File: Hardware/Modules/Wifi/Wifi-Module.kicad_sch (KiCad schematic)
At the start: 9 parts, among them J3 Conn_01x01_Pin, J4 B4B-EH-A, J5 Conn_01x10, J6 Conn_01x10, J7 B4B-EH-A, U1 ESP32-C6-MINI-1-H4, U2 TLV70033_SOT23-5

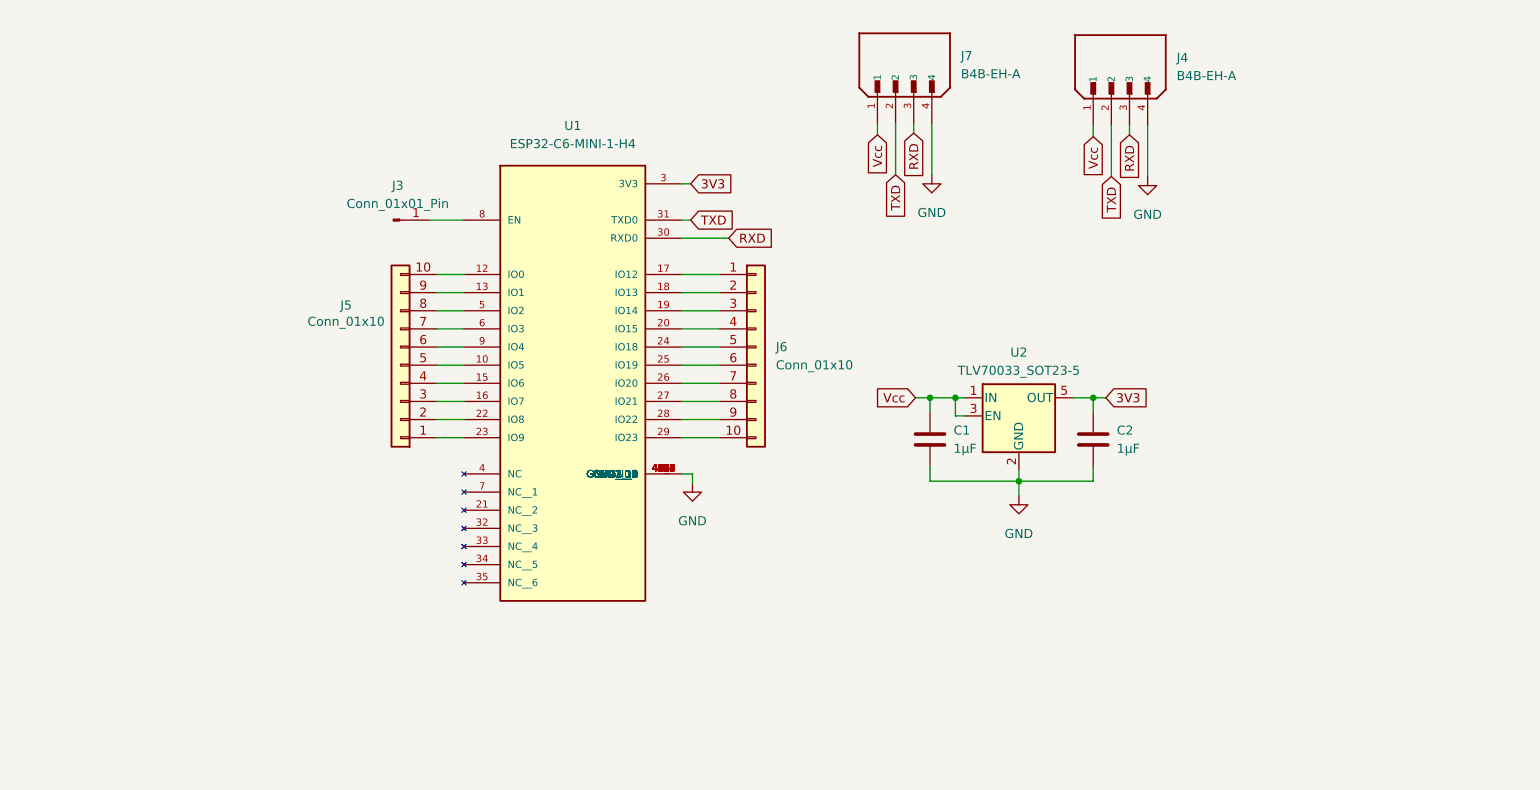
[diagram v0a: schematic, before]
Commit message: Correction in the Wifi Module
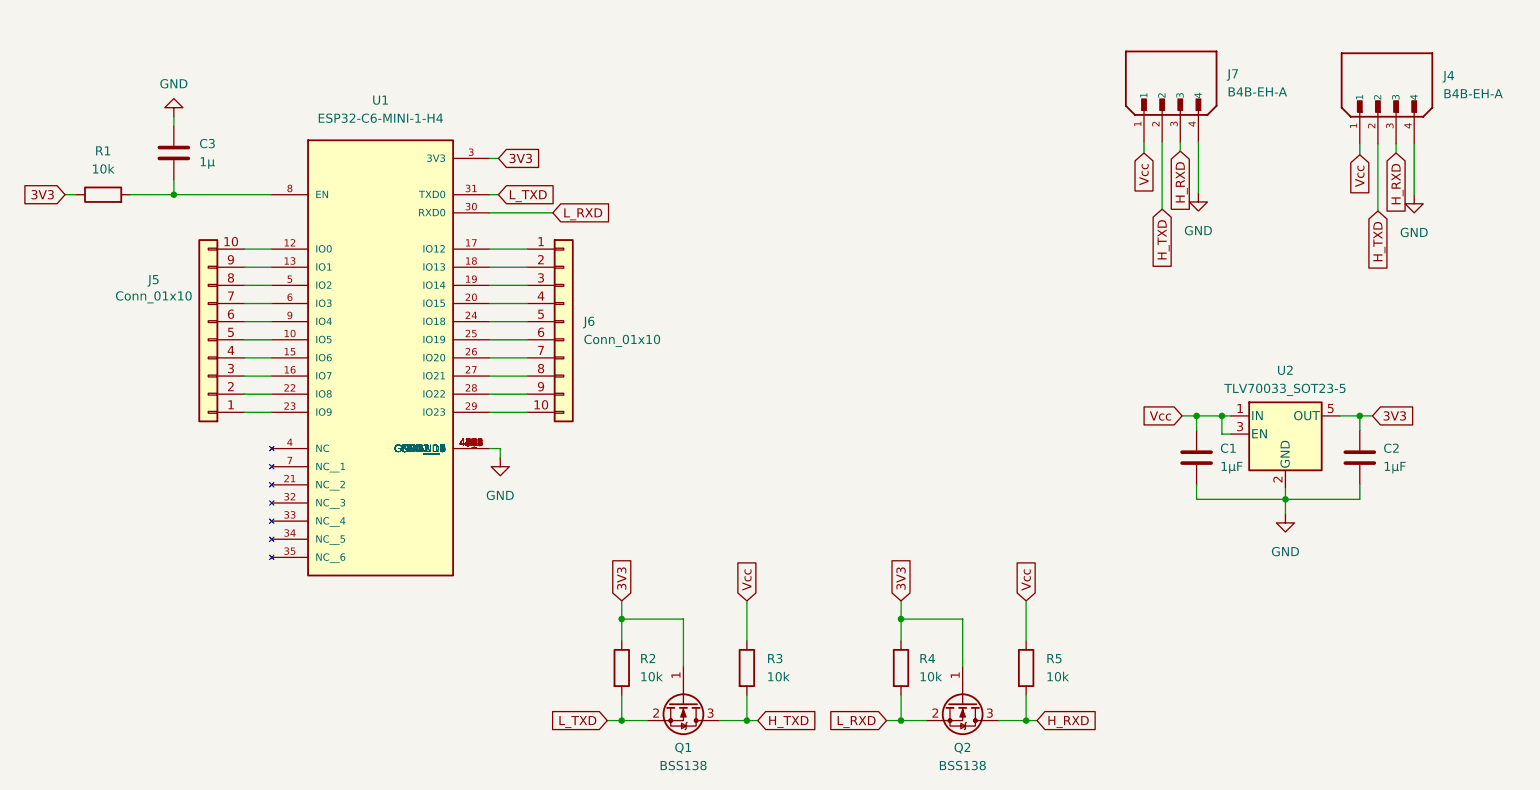
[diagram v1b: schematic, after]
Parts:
- removed J3: Conn_01x01_Pin, Connector_PinHeader_2.54mm:PinHeader_1x01_P2.54mm_Vertical, symbol Connector:Conn_01x01_Pin
- added C3: 1µ, Capacitor_SMD:C_0603_1608Metric_Pad1.08x0.95mm_HandSolder, symbol Device:C
- added Q1, Q2: BSS138, Package_TO_SOT_SMD:SOT-23, symbol Transistor_FET:BSS138
- added R1, R2, R3, R4, R5: 10k, Resistor_SMD:R_0603_1608Metric_Pad0.98x0.95mm_HandSolder, symbol Device:R
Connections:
- net 3V3: now also Q1.1 (G), Q2.1 (G), R1.1, R2.1, R4.1
- net GND: now also C3.1
- net Vcc: now also R3.1, R5.1
- net at U1.8 (EN): now also C3.2, R1.2
- net RXD renamed H_RXD
- net H_RXD: now also Q2.3 (D), R5.2; no longer U1.30 (RXD0)
- net TXD renamed H_TXD
- net H_TXD: now also Q1.3 (D), R3.2; no longer U1.31 (TXD0)
- new net L_RXD: Q2.2 (S), R4.2, U1.30 (RXD0)
- new net L_TXD: Q1.2 (S), R2.2, U1.31 (TXD0)
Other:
- moved on the sheet: C1, C2, J4, J5, J6, J7, U1, U2

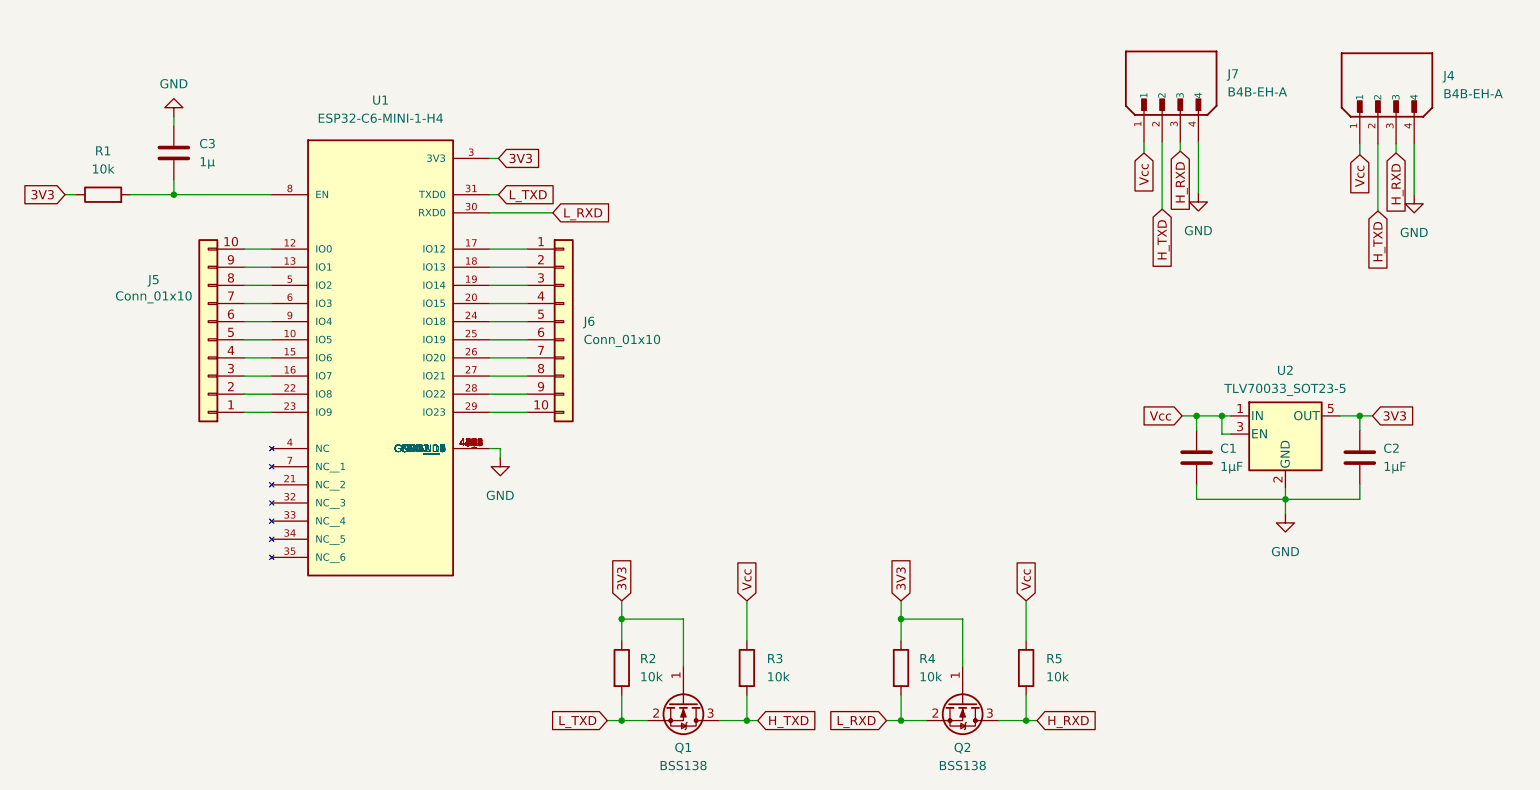
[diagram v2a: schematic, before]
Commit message: Finall Version of the Wifi-Module (correct mistakes))
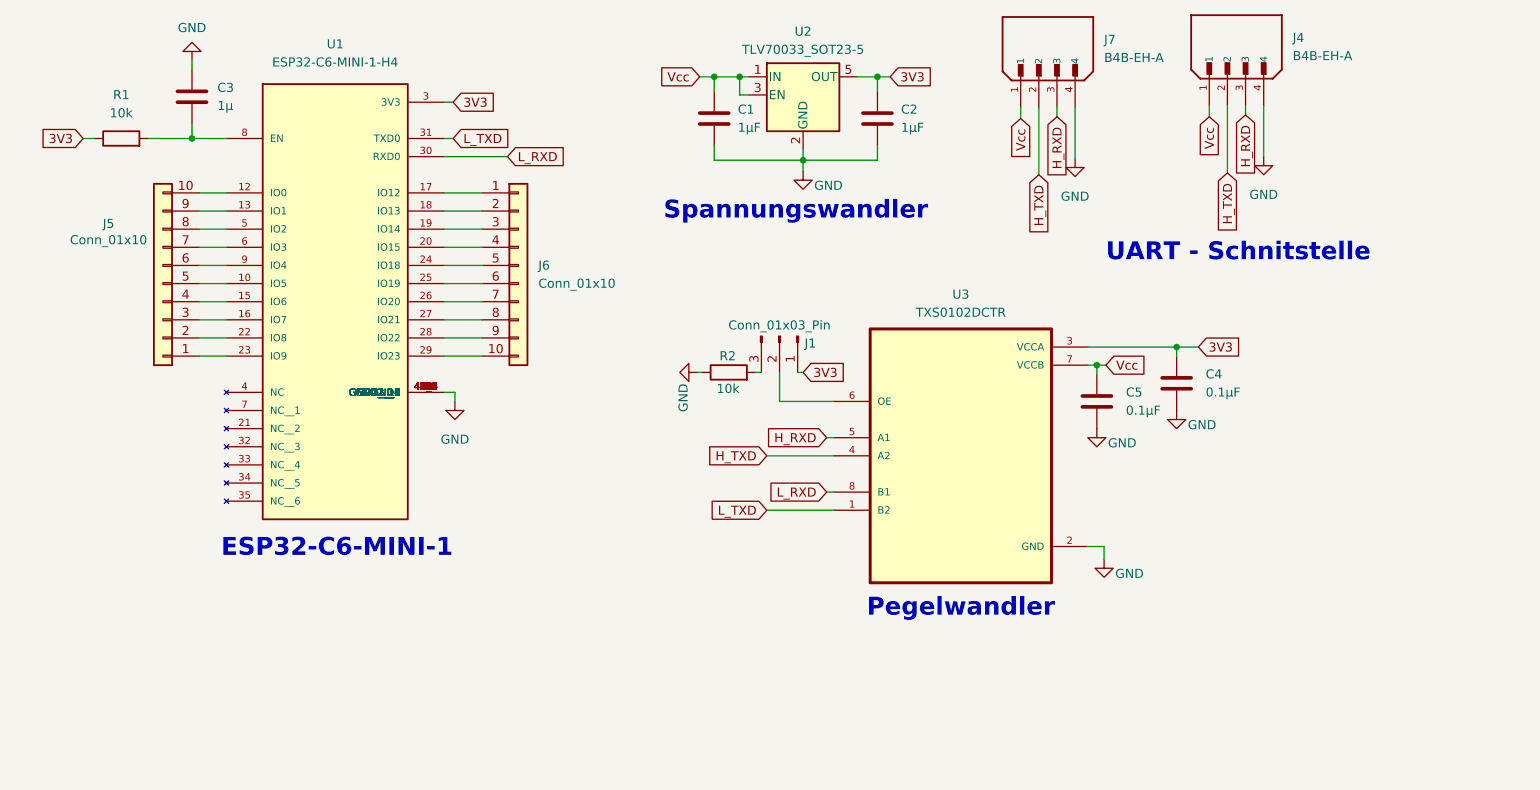
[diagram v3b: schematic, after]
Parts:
- removed Q1, Q2: BSS138, Package_TO_SOT_SMD:SOT-23, symbol Transistor_FET:BSS138
- removed R3, R4, R5: 10k, Resistor_SMD:R_0603_1608Metric_Pad0.98x0.95mm_HandSolder, symbol Device:R
- added C4, C5: 0.1µF, Capacitor_SMD:C_0603_1608Metric_Pad1.08x0.95mm_HandSolder, symbol Device:C
- added J1: Conn_01x03_Pin, Connector_PinHeader_2.54mm:PinHeader_1x03_P2.54mm_Vertical, symbol Connector:Conn_01x03_Pin
- added U3: TXS0102DCTR, Modular-Elektronics-Toolkit-Global-Libary:TXS0102DCTR, symbol Modular_Electronics_Toolkit_sym:TXS0102DCTR
- J4, J7: footprint Modular-Electronics-Toolkit-BP:JST_B4B-EH-A -> Modular-Elektronics-Toolkit-Global-Libary:JST_B4B-EH-A
- U1: footprint Modular-Electronics-Toolkit-BP:XCVR_ESP32-C6-MINI-1-H4 -> Modular-Elektronics-Toolkit-Global-Libary:XCVR_ESP32-C6-MINI-1-H4
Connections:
- net 3V3: now also C4.2, J1.1 (Pin_1), U3.3 (VCCA); no longer R2.1
- net GND: now also R2.1, C4.1, C5.1, U3.2 (GND)
- net H_RXD: now also U3.5 (A1)
- net H_TXD: now also U3.4 (A2)
- net L_RXD: now also U3.8 (B1)
- net L_TXD: now also U3.1 (B2); no longer R2.2
- net Vcc: now also C5.2, U3.7 (VCCB)
- new net: J1.2 (Pin_2), U3.6 (OE)
- new net: J1.3 (Pin_3), R2.2
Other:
- note added: "ESP32-C6-MINI-1"
- note added: "Pegelwandler"
- note added: "Spannungswandler"
- note added: "UART - Schnitstelle"
- moved on the sheet: C1, C2, C3, J4, J5, J6, J7, R1, U1, U2
